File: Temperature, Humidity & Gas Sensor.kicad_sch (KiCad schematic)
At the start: 7 parts, among them U14 BME690

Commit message: PCB Routing
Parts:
- renumbered C29 to C37, C30 to C38, U14 to U15
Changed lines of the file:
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@@
 		(dnp no)
 		(fields_autoplaced yes)
-		(property "Reference" "#PWR074"
+		(property "Reference" "#PWR083"
 			(at 101.6 104.14 0)
 			(effects
@@
 			(project ""
 				(path "/c9a8ff63-a0d1-4125-9dd1-40fb53daf536/cc882cab-fb20-4552-b867-43569dfc2d06"
-					(reference "#PWR074")
+					(reference "#PWR083")
 					(unit 1)
 				)
@@
 		(dnp no)
 		(fields_autoplaced yes)
-		(property "Reference" "C29"
+		(property "Reference" "C37"
 			(at 92.71 88.8999 0)
 			(effects
@@
 			(project "Precision Clock"
 				(path "/c9a8ff63-a0d1-4125-9dd1-40fb53daf536/cc882cab-fb20-4552-b867-43569dfc2d06"
-					(reference "C29")
+					(reference "C37")
 					(unit 1)
 				)
@@
 		(dnp no)
 		(fields_autoplaced yes)
-		(property "Reference" "#PWR079"
+		(property "Reference" "#PWR088"
 			(at 157.48 86.36 0)
 			(effects
@@
 			(project "Precision Clock"
 				(path "/c9a8ff63-a0d1-4125-9dd1-40fb53daf536/cc882cab-fb20-4552-b867-43569dfc2d06"
-					(reference "#PWR079")
+					(reference "#PWR088")
 					(unit 1)
 				)
@@
 		(dnp no)
 		(fields_autoplaced yes)
-		(property "Reference" "#PWR077"
+		(property "Reference" "#PWR086"
 			(at 149.86 93.98 0)
 			(effects
@@
 			(project ""
 				(path "/c9a8ff63-a0d1-4125-9dd1-40fb53daf536/cc882cab-fb20-4552-b867-43569dfc2d06"
-					(reference "#PWR077")
+					(reference "#PWR086")
 					(unit 1)
 				)
@@
 		(dnp no)
 		(fields_autoplaced yes)
-		(property "Reference" "#PWR078"
+		(property "Reference" "#PWR087"
 			(at 149.86 111.76 0)
 			(effects
@@
 			(project "Precision Clock"
 				(path "/c9a8ff63-a0d1-4125-9dd1-40fb53daf536/cc882cab-fb20-4552-b867-43569dfc2d06"
-					(reference "#PWR078")
+					(reference "#PWR087")
 					(unit 1)
 				)
@@
 		(dnp no)
 		(fields_autoplaced yes)
-		(property "Reference" "C30"
+		(property "Reference" "C38"
 			(at 105.41 88.8999 0)
 			(effects
@@
 			(project ""
 				(path "/c9a8ff63-a0d1-4125-9dd1-40fb53daf536/cc882cab-fb20-4552-b867-43569dfc2d06"
-					(reference "C30")
+					(reference "C38")
 					(unit 1)
 				)
@@
 		(dnp no)
 		(fields_autoplaced yes)
-		(property "Reference" "#PWR073"
+		(property "Reference" "#PWR082"
 			(at 88.9 104.14 0)
 			(effects
@@
 			(project "Precision Clock"
 				(path "/c9a8ff63-a0d1-4125-9dd1-40fb53daf536/cc882cab-fb20-4552-b867-43569dfc2d06"
-					(reference "#PWR073")
+					(reference "#PWR082")
 					(unit 1)
 				)
@@
 		(dnp no)
 		(fields_autoplaced yes)
-		(property "Reference" "#PWR076"
+		(property "Reference" "#PWR085"
 			(at 129.54 119.38 0)
 			(effects
@@
 			(project ""
 				(path "/c9a8ff63-a0d1-4125-9dd1-40fb53daf536/cc882cab-fb20-4552-b867-43569dfc2d06"
-					(reference "#PWR076")
+					(reference "#PWR085")
 					(unit 1)
 				)
@@
 		(dnp no)
 		(fields_autoplaced yes)
-		(property "Reference" "#PWR075"
+		(property "Reference" "#PWR084"
 			(at 127 83.82 0)
 			(effects
@@
 			(project ""
 				(path "/c9a8ff63-a0d1-4125-9dd1-40fb53daf536/cc882cab-fb20-4552-b867-43569dfc2d06"
-					(reference "#PWR075")
+					(reference "#PWR084")
 					(unit 1)
 				)
@@
 		(dnp no)
 		(fields_autoplaced yes)
-		(property "Reference" "#PWR080"
+		(property "Reference" "#PWR089"
 			(at 168.91 86.36 0)
 			(effects
@@
 			(project "Precision Clock"
 				(path "/c9a8ff63-a0d1-4125-9dd1-40fb53daf536/cc882cab-fb20-4552-b867-43569dfc2d06"
-					(reference "#PWR080")
+					(reference "#PWR089")
 					(unit 1)
 				)
@@
 		(dnp no)
 		(fields_autoplaced yes)
-		(property "Reference" "U14"
+		(property "Reference" "U15"
 			(at 119.38 95.2499 0)
 			(effects
@@
 			(project ""
 				(path "/c9a8ff63-a0d1-4125-9dd1-40fb53daf536/cc882cab-fb20-4552-b867-43569dfc2d06"
-					(reference "U14")
-					(unit 1)
-				)
+					(reference "U15")
+					(unit 1)
+				)

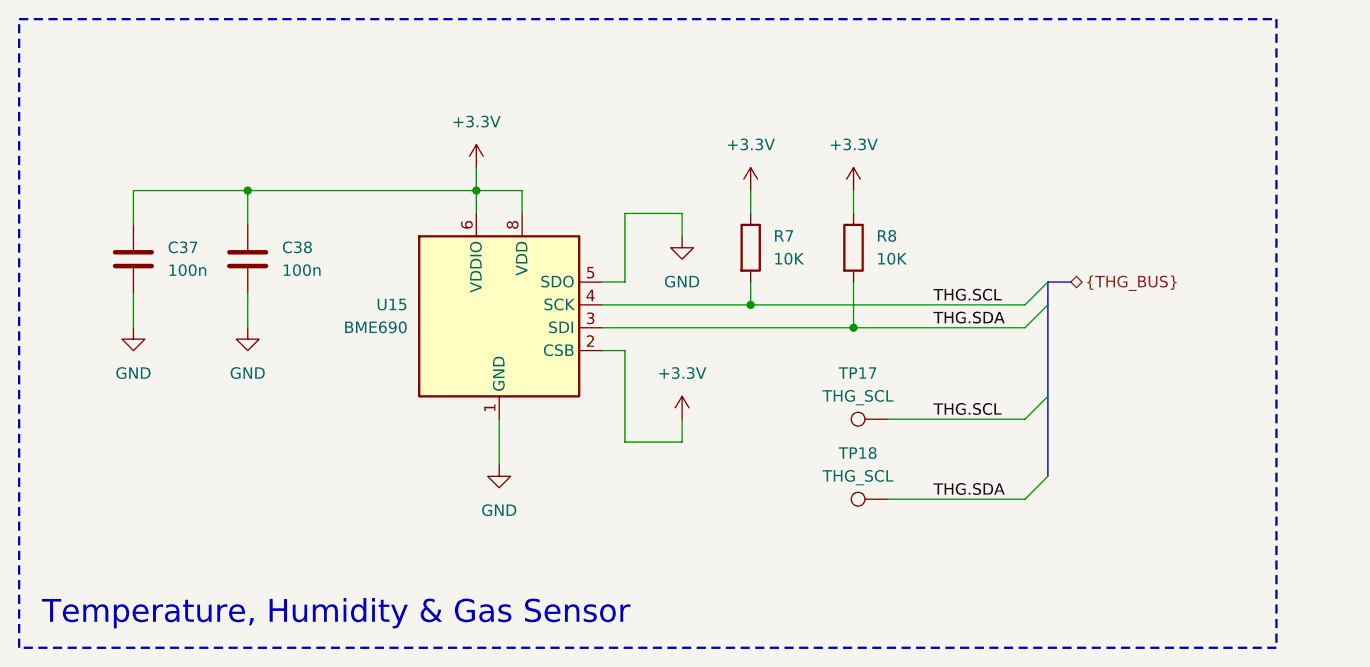
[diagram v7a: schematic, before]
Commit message: Footprints added
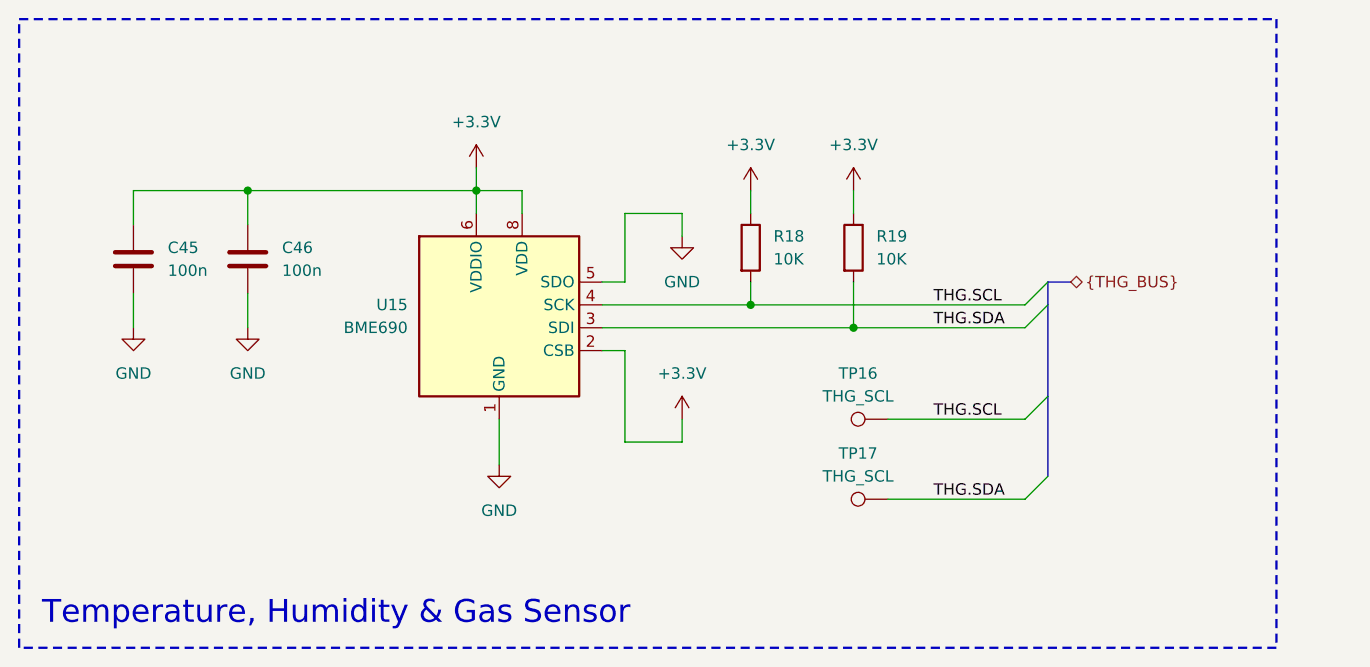
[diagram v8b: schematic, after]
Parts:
- renumbered C37 to C45, C38 to C46, R7 to R18, R8 to R19, TP17 to TP16, TP18 to TP17
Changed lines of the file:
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@@
 		(dnp no)
 		(fields_autoplaced yes)
-		(property "Reference" "#PWR083"
+		(property "Reference" "#PWR0105"
 			(at 101.6 104.14 0)
 			(effects
@@
 			(project ""
 				(path "/c9a8ff63-a0d1-4125-9dd1-40fb53daf536/cc882cab-fb20-4552-b867-43569dfc2d06"
-					(reference "#PWR083")
+					(reference "#PWR0105")
 					(unit 1)
 				)
@@
 		(dnp no)
 		(fields_autoplaced yes)
-		(property "Reference" "C37"
+		(property "Reference" "C45"
 			(at 92.71 88.8999 0)
 			(effects
@@
 			(project "Precision Clock"
 				(path "/c9a8ff63-a0d1-4125-9dd1-40fb53daf536/cc882cab-fb20-4552-b867-43569dfc2d06"
-					(reference "C37")
+					(reference "C45")
 					(unit 1)
 				)
@@
 		(dnp no)
 		(fields_autoplaced yes)
-		(property "Reference" "TP17"
+		(property "Reference" "TP16"
 			(at 169.418 102.87 90)
 			(effects
@@
 			(project ""
 				(path "/c9a8ff63-a0d1-4125-9dd1-40fb53daf536/cc882cab-fb20-4552-b867-43569dfc2d06"
-					(reference "TP17")
+					(reference "TP16")
 					(unit 1)
 				)
@@
 		(dnp no)
 		(fields_autoplaced yes)
-		(property "Reference" "#PWR088"
+		(property "Reference" "#PWR0110"
 			(at 157.48 86.36 0)
 			(effects
@@
 			(project "Precision Clock"
 				(path "/c9a8ff63-a0d1-4125-9dd1-40fb53daf536/cc882cab-fb20-4552-b867-43569dfc2d06"
-					(reference "#PWR088")
+					(reference "#PWR0110")
 					(unit 1)
 				)
@@
 		(dnp no)
 		(fields_autoplaced yes)
-		(property "Reference" "R8"
+		(property "Reference" "R19"
 			(at 171.45 87.6299 0)
 			(effects
@@
 			(project "Precision Clock"
 				(path "/c9a8ff63-a0d1-4125-9dd1-40fb53daf536/cc882cab-fb20-4552-b867-43569dfc2d06"
-					(reference "R8")
+					(reference "R19")
 					(unit 1)
 				)
@@
 		(dnp no)
 		(fields_autoplaced yes)
-		(property "Reference" "#PWR086"
+		(property "Reference" "#PWR0108"
 			(at 149.86 93.98 0)
 			(effects
@@
 			(project ""
 				(path "/c9a8ff63-a0d1-4125-9dd1-40fb53daf536/cc882cab-fb20-4552-b867-43569dfc2d06"
-					(reference "#PWR086")
+					(reference "#PWR0108")
 					(unit 1)
 				)
@@
 		(dnp no)
 		(fields_autoplaced yes)
-		(property "Reference" "#PWR087"
+		(property "Reference" "#PWR0109"
 			(at 149.86 111.76 0)
 			(effects
@@
 			(project "Precision Clock"
 				(path "/c9a8ff63-a0d1-4125-9dd1-40fb53daf536/cc882cab-fb20-4552-b867-43569dfc2d06"
-					(reference "#PWR087")
+					(reference "#PWR0109")
 					(unit 1)
 				)
@@
 		(dnp no)
 		(fields_autoplaced yes)
-		(property "Reference" "C38"
+		(property "Reference" "C46"
 			(at 105.41 88.8999 0)
 			(effects
@@
 			(project ""
 				(path "/c9a8ff63-a0d1-4125-9dd1-40fb53daf536/cc882cab-fb20-4552-b867-43569dfc2d06"
-					(reference "C38")
+					(reference "C46")
 					(unit 1)
 				)
@@
 		(dnp no)
 		(fields_autoplaced yes)
-		(property "Reference" "#PWR082"
+		(property "Reference" "#PWR0104"
 			(at 88.9 104.14 0)
 			(effects
@@
 			(project "Precision Clock"
 				(path "/c9a8ff63-a0d1-4125-9dd1-40fb53daf536/cc882cab-fb20-4552-b867-43569dfc2d06"
-					(reference "#PWR082")
+					(reference "#PWR0104")
 					(unit 1)
 				)
@@
 		(dnp no)
 		(fields_autoplaced yes)
-		(property "Reference" "R7"
+		(property "Reference" "R18"
 			(at 160.02 87.6299 0)
 			(effects
@@
 			(project ""
 				(path "/c9a8ff63-a0d1-4125-9dd1-40fb53daf536/cc882cab-fb20-4552-b867-43569dfc2d06"
-					(reference "R7")
+					(reference "R18")
 					(unit 1)
 				)
@@
 		(dnp no)
 		(fields_autoplaced yes)
-		(property "Reference" "#PWR085"
+		(property "Reference" "#PWR0107"
 			(at 129.54 119.38 0)
 			(effects
@@
 			(project ""
 				(path "/c9a8ff63-a0d1-4125-9dd1-40fb53daf536/cc882cab-fb20-4552-b867-43569dfc2d06"
-					(reference "#PWR085")
+					(reference "#PWR0107")
 					(unit 1)
 				)
@@
 		(dnp no)
 		(fields_autoplaced yes)
-		(property "Reference" "#PWR084"
+		(property "Reference" "#PWR0106"
 			(at 127 83.82 0)
 			(effects
@@
 			(project ""
 				(path "/c9a8ff63-a0d1-4125-9dd1-40fb53daf536/cc882cab-fb20-4552-b867-43569dfc2d06"
-					(reference "#PWR084")
+					(reference "#PWR0106")
 					(unit 1)
 				)
@@
 		(dnp no)
 		(fields_autoplaced yes)
-		(property "Reference" "#PWR089"
+		(property "Reference" "#PWR0111"
 			(at 168.91 86.36 0)
 			(effects
@@
 			(project "Precision Clock"
 				(path "/c9a8ff63-a0d1-4125-9dd1-40fb53daf536/cc882cab-fb20-4552-b867-43569dfc2d06"
-					(reference "#PWR089")
+					(reference "#PWR0111")
 					(unit 1)
 				)
@@
 		(dnp no)
 		(fields_autoplaced yes)
-		(property "Reference" "TP18"
+		(property "Reference" "TP17"
 			(at 169.418 111.76 90)
 			(effects
@@
 			(project "Precision Clock"
 				(path "/c9a8ff63-a0d1-4125-9dd1-40fb53daf536/cc882cab-fb20-4552-b867-43569dfc2d06"
-					(reference "TP18")
-					(unit 1)
-				)
+					(reference "TP17")
+					(unit 1)
+				)
